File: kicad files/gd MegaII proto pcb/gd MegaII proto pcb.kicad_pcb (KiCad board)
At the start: 2 copper layers, 75 parts, among them J1 ABDIR, J2 ABEN, J3 FLIP, J4 DBDIR, J5 DBEN, J6 VGC Extra, J7 Bald-Ext-1, J8 VGC Extra, J9 Address, U1 Apple_MEGA_II, U2 DRAM64KX4, U3 74HCT245, U4 DRAM64KX4, U5 74HCT245, U6 74HCT86, U7 DRAM64KX4, U8 74HCT245, U9 DRAM64KX4

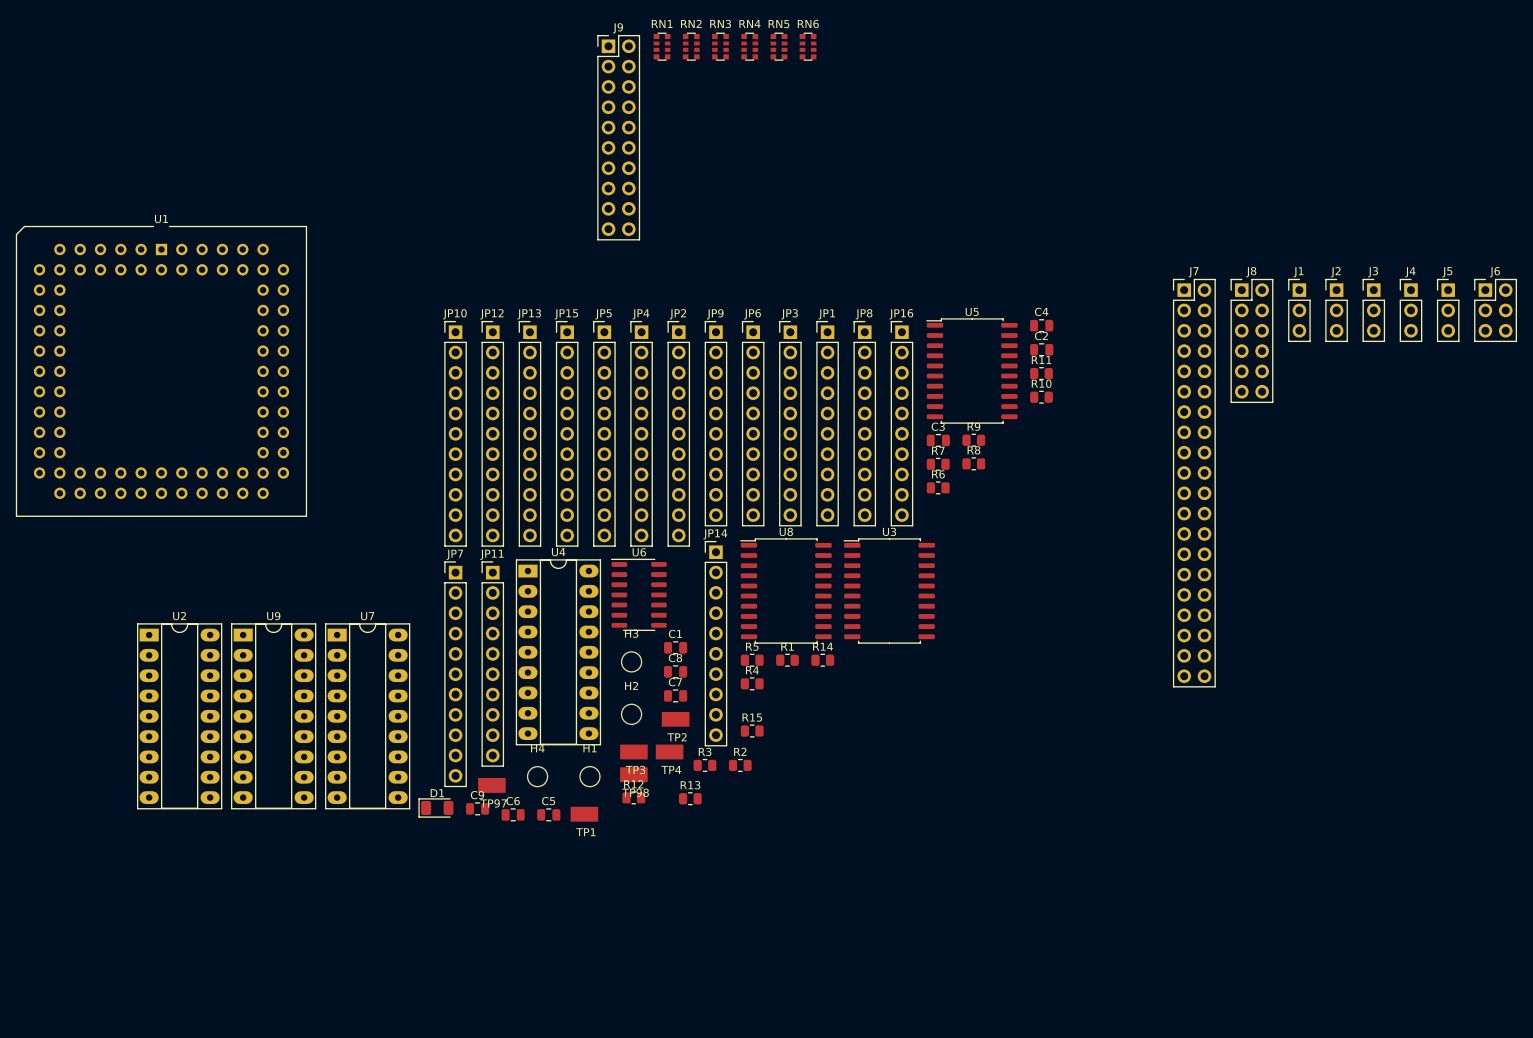
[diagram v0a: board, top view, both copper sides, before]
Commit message: MegaII 0 unrouted but 40+ DRC errors. KiCad doesn't like any of my via placements.
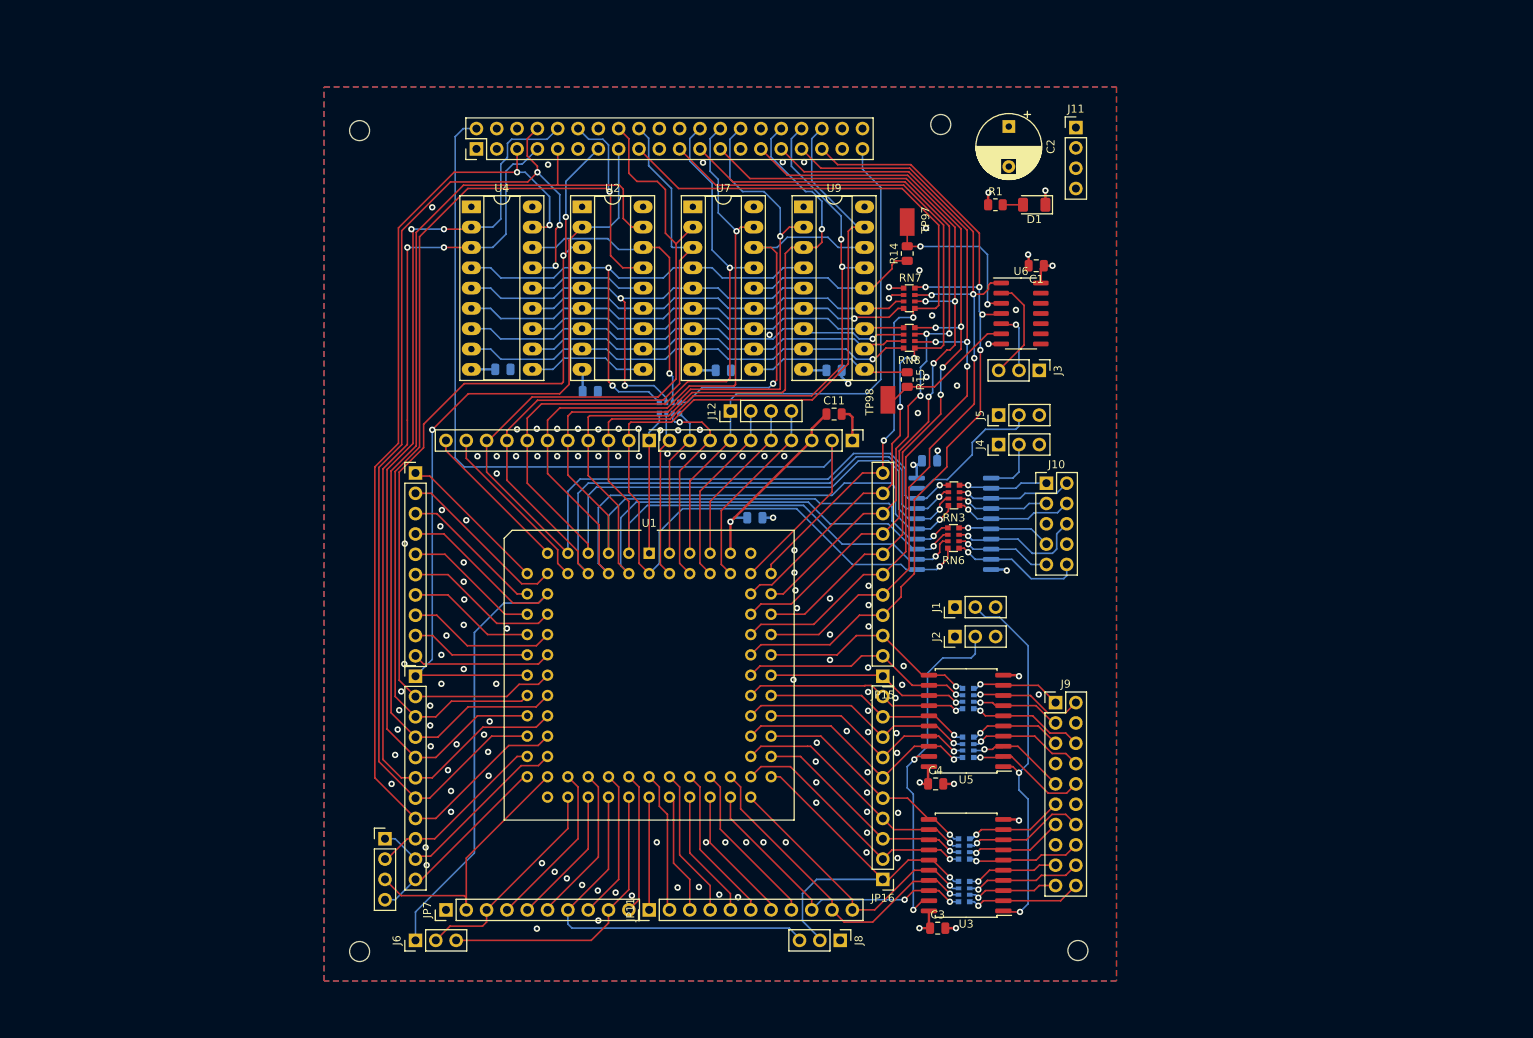
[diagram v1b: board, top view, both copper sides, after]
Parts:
- removed JP10, JP2: P22-32, Connector_PinHeader_2.54mm:PinHeader_1x11_P2.54mm_Vertical
- removed JP13, JP5: P43-53, Connector_PinHeader_2.54mm:PinHeader_1x11_P2.54mm_Vertical
- removed JP14, JP6: P75-84, Connector_PinHeader_2.54mm:PinHeader_1x10_P2.54mm_Vertical
- removed JP9: P12-21, Connector_PinHeader_2.54mm:PinHeader_1x10_P2.54mm_Vertical
- removed R10, R11, R12, R13, R2, R3, R4, R5, R6, R7, R8, R9: 100, Resistor_SMD:R_0805_2012Metric
- removed TP1, TP2, TP3, TP4: TestPoint, My Libraries:Harwin-S1751-46-Test-Point
- added C10: 10uF, Capacitor_SMD:C_0805_2012Metric, B.Cu at (142.7, 86.9)
- added C11: 1uF, Capacitor_SMD:C_0805_2012Metric, F.Cu at (152.7, 73.9)
- added J10: Data, Connector_PinHeader_2.54mm:PinHeader_2x05_P2.54mm_Vertical, F.Cu at (179.2, 82.5)
- added J11: PWR, Connector_PinHeader_2.54mm:PinHeader_1x04_P2.54mm_Vertical, F.Cu at (182.9, 38.1)
- added J12: CLKS, Connector_PinHeader_2.54mm:PinHeader_1x04_P2.54mm_Vertical, F.Cu at (139.7, 73.5)
- added RN7: 100, Resistor_SMD:R_Array_Convex_4x0612, F.Cu at (162.1, 59.4)
- added RN8: 100, Resistor_SMD:R_Array_Convex_4x0612, F.Cu at (162.1, 64.4)
- added RN9: 100, Resistor_SMD:R_Array_Convex_4x0612, B.Cu at (132.1, 73.2)
- C2: value 10uF -> 100uF; footprint Capacitor_SMD:C_0805_2012Metric -> Capacitor_THT:CP_Radial_D8.0mm_P5.00mm
- C5, C6, C7, C8, C9, RN1, RN2, RN4, RN5, U8: moved to B.Cu
- J6: value VGC Extra -> VGC Extra 1; footprint Connector_PinHeader_2.54mm:PinHeader_2x03_P2.54mm_Vertical -> Connector_PinHeader_2.54mm:PinHeader_1x03_P2.54mm_Vertical
- J8: value VGC Extra -> VGC Extra 2; footprint Connector_PinHeader_2.54mm:PinHeader_2x06_P2.54mm_Vertical -> Connector_PinHeader_2.54mm:PinHeader_1x03_P2.54mm_Vertical
- JP1: value P12-21 -> RGB Binary; footprint Connector_PinHeader_2.54mm:PinHeader_1x10_P2.54mm_Vertical -> Connector_PinHeader_2.54mm:PinHeader_1x04_P2.54mm_Vertical
- JP11: value P33-42 -> P64-74; footprint Connector_PinHeader_2.54mm:PinHeader_1x10_P2.54mm_Vertical -> Connector_PinHeader_2.54mm:PinHeader_1x11_P2.54mm_Vertical
- JP12: value P01-11 -> P54-63; footprint Connector_PinHeader_2.54mm:PinHeader_1x11_P2.54mm_Vertical -> Connector_PinHeader_2.54mm:PinHeader_1x10_P2.54mm_Vertical
- JP3: value P33-42 -> P54-63
- JP4: value P01-11 -> P64-74
- JP7: value P64-74 -> P54-63; footprint Connector_PinHeader_2.54mm:PinHeader_1x11_P2.54mm_Vertical -> Connector_PinHeader_2.54mm:PinHeader_1x10_P2.54mm_Vertical
- JP8: value P54-63 -> P64-74; footprint Connector_PinHeader_2.54mm:PinHeader_1x10_P2.54mm_Vertical -> Connector_PinHeader_2.54mm:PinHeader_1x11_P2.54mm_Vertical
- moved J6 156.5 mm to (100.3, 139.7), turned to 90 degrees
- moved RN5 108.1 mm to (168.9, 133.6), turned to 180 degrees
- moved D1 106.1 mm to (177.7, 47.8), turned to 180 degrees
- moved RN2 105.9 mm to (168.9, 128.3), turned to 180 degrees
- moved J9 99.3 mm to (180.3, 110.0)
- moved J8 95.5 mm to (153.4, 139.7), turned to 270 degrees
- moved RN4 91.7 mm to (169.4, 115.6), turned to 180 degrees
- moved J7 90.2 mm to (108.0, 40.8), turned to 90 degrees
- moved RN1 90.0 mm to (169.4, 109.5), turned to 180 degrees
- moved U9 88.2 mm to (148.8, 48.0)
- moved TP97 87.5 mm to (161.8, 49.9), turned to 90 degrees
- moved JP1 84.1 mm to (96.5, 127.0)
- moved H2 83.2 mm to (166.0, 37.7)
- moved U2 76.1 mm to (121.2, 48.0)
- moved H3 74.6 mm to (93.3, 38.5)
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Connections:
- C1 pad 1: VDD -> +5V
- C2 pad 1: VDD -> +5V
- C3 pad 1: VDD -> +5V
- C4 pad 1: VDD -> +5V
- C5 pad 1: VDD -> +5V
- C6 pad 1: VDD -> +5V
- C7 pad 1: VDD -> +5V
- C8 pad 1: VDD -> +5V
- C9 pad 1: VDD -> +5V
- J1 pad 1: VDD -> +5V
- J2 pad 1: VDD -> +5V
- J4 pad 1: VDD -> +5V
- J5 pad 1: VDD -> +5V
- J6 pad 2: /IRQ -> /RESET
- J6 pad 3: /RESET -> /R-W
- J7 pad 30: Net-(J7-Pad30) -> GND
- J8 pad 1: Net-(J8-Pad1) -> GND
- J8 pad 2: Net-(J8-Pad2) -> /BA12
- J8 pad 3: Net-(J8-Pad3) -> /M2SEL
- JP1 pad 1: /SPKR -> /RGB4
- JP1 pad 2: /KSEL1 -> /RGB8
- JP1 pad 3: /KSEL2 -> /RGB1
- JP1 pad 4: /IRQ -> /RGB2
- JP11 pad 1: GND -> /S1
- JP11 pad 10: /S0 -> /BA14
- JP11 pad 2: /RGB1 -> /S2
- JP11 pad 3: /RESET -> /S3
- JP11 pad 4: /MDI-MDO -> /S4
- JP11 pad 5: /RCMEN -> /S5
- JP11 pad 6: /DMA -> /RMBK
- JP11 pad 7: /M2SEL -> /WINDOW
- JP11 pad 8: /INH -> /SYNC
- JP11 pad 9: /R-W -> /BA15
- JP12 pad 1: /RAMWE -> GND
- JP12 pad 10: /PDLTRIG -> /RAS
- JP12 pad 2: /MD7 -> /14M
- JP12 pad 3: /MD6 -> +5V
- JP12 pad 4: /MD5 -> /7M
- JP12 pad 5: /MD4 -> /CREF
- JP12 pad 6: /MD3 -> /Q3
- JP12 pad 7: /MD2 -> /PH#
- JP12 pad 8: /MD1 -> /CASA
- JP12 pad 9: /MD0 -> /CASM
- JP15 pad 1: /A2 -> /BA2
- JP15 pad 2: /A1 -> /BA1
- JP15 pad 3: /A0 -> /BA0
- JP16 pad 1: /A12 -> /BA12
- JP16 pad 10: /A3 -> /BA3
- JP16 pad 2: /A11 -> /BA11
- JP16 pad 3: /A10 -> /BA10
- JP16 pad 4: /A9 -> /BA9
- JP16 pad 5: /A8 -> /BA8
- JP16 pad 6: /A7 -> /BA7
- JP16 pad 7: /A6 -> /BA6
- JP16 pad 8: /A5 -> /BA5
- JP16 pad 9: /A4 -> /BA4
- JP3 pad 1: GND -> /SPKR
- JP3 pad 10: /S0 -> /SERVIDEO
- JP3 pad 2: /RGB1 -> /KSEL1
- JP3 pad 3: /RESET -> /KSEL2
- JP3 pad 4: /MDI-MDO -> /IRQ
- JP3 pad 5: /RCMEN -> /X0
- JP3 pad 6: /DMA -> /X1
- JP3 pad 7: /M2SEL -> /Y0
- JP3 pad 8: /INH -> /Y1
- JP3 pad 9: /R-W -> /MSW
- JP4 pad 1: /RAMWE -> /AD0
- JP4 pad 10: /PDLTRIG -> /RGB4
- JP4 pad 11: /C060-67 -> /RGB2
- JP4 pad 2: /MD7 -> /AD1
- JP4 pad 3: /MD6 -> /AD2
- JP4 pad 4: /MD5 -> /AD3
- JP4 pad 5: /MD4 -> /AD4
- JP4 pad 6: /MD3 -> /AD5
- JP4 pad 7: /MD2 -> /AD6
- JP4 pad 8: /MD1 -> /AD7
- JP4 pad 9: /MD0 -> /RGB8
- JP7 pad 1: /A2 -> GND
- JP7 pad 10: /RA1 -> /S0
- JP7 pad 2: /A1 -> /RGB1
- JP7 pad 3: /A0 -> /RESET
- JP7 pad 4: /RA7 -> /MDI-MDO
- JP7 pad 5: /RA6 -> /ROMEN
- JP7 pad 6: /RA5 -> /DMA
- JP7 pad 7: /RA4 -> /M2SEL
- JP7 pad 8: /RA3 -> /INH
- JP7 pad 9: /RA2 -> /R-W
- JP8 pad 1: /A12 -> /RAMWE
- JP8 pad 10: /A3 -> /PDLTRIG
- JP8 pad 2: /A11 -> /MD7
- JP8 pad 3: /A10 -> /MD6
- JP8 pad 4: /A9 -> /MD5
- JP8 pad 5: /A8 -> /MD4
- JP8 pad 6: /A7 -> /MD3
- JP8 pad 7: /A6 -> /MD2
- JP8 pad 8: /A5 -> /MD1
- JP8 pad 9: /A4 -> /MD0
- R1 pad 1: VDD -> +5V
- RN3 pad 1: /D0 -> /D3
- RN3 pad 2: /D1 -> /D2
- RN3 pad 3: /D2 -> /D1
- RN3 pad 4: /D3 -> /D0
- RN3 pad 5: /MD3 -> /MD0
- RN3 pad 6: /MD2 -> /MD1
- RN3 pad 7: /MD1 -> /MD2
- RN3 pad 8: /MD0 -> /MD3
- RN6 pad 1: /D4 -> /D7
- RN6 pad 2: /D5 -> /D6
- RN6 pad 3: /D6 -> /D5
- RN6 pad 4: /D7 -> /D4
- RN6 pad 5: /MD7 -> /MD4
- RN6 pad 6: /MD6 -> /MD5
- RN6 pad 7: /MD5 -> /MD6
- RN6 pad 8: /MD4 -> /MD7
- U1 pad 77: VDD -> +5V
- U2 pad 9: VDD -> +5V
- U3 pad 20: VDD -> +5V
- U4 pad 9: VDD -> +5V
- U5 pad 20: VDD -> +5V
- U6 pad 14: (no net) -> +5V
- U6 pad 7: (no net) -> GND
- U7 pad 9: VDD -> +5V
- U8 pad 11: /MD0 -> /MD7
- U8 pad 12: /MD1 -> /MD6
- U8 pad 13: /MD2 -> /MD5
- U8 pad 14: /MD3 -> /MD4
- U8 pad 15: /MD4 -> /MD3
- U8 pad 16: /MD5 -> /MD2
- U8 pad 17: /MD6 -> /MD1
- U8 pad 18: /MD7 -> /MD0
- U8 pad 2: /D7 -> /D0
- U8 pad 20: VDD -> +5V
- U8 pad 3: /D6 -> /D1
- U8 pad 4: /D5 -> /D2
- U8 pad 5: /D4 -> /D3
- U8 pad 6: /D3 -> /D4
- U8 pad 7: /D2 -> /D5
- U8 pad 8: /D1 -> /D6
- U8 pad 9: /D0 -> /D7
- U9 pad 9: VDD -> +5V
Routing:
- net /MD1: track 0.00 -> 147.7 mm, vias 0 -> 1
- net /MD0: track 0.00 -> 147.2 mm, vias 0 -> 1
- net /MD2: track 0.00 -> 145.5 mm, vias 0 -> 2
- net /MD3: track 0.00 -> 144.1 mm, vias 0 -> 2
- net /MD5: track 0.00 -> 140.1 mm, vias 0 -> 2
- net /MD4: track 0.00 -> 139.5 mm, vias 0 -> 2
- net /MD6: track 0.00 -> 134.2 mm, vias 0 -> 3
- net /AD6: track 0.00 -> 133.8 mm, vias 0 -> 3
- net /MD7: track 0.00 -> 133.2 mm, vias 0 -> 1
- net /AD7: track 0.00 -> 129.7 mm, vias 0 -> 2
- net /AD2: track 0.00 -> 127.1 mm, vias 0 -> 1
- net /AD3: track 0.00 -> 124.0 mm
- net /AD5: track 0.00 -> 116.0 mm, vias 0 -> 2
- net /14M: track 0.00 -> 114.4 mm
- net /AD4: track 0.00 -> 113.6 mm, vias 0 -> 2
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- added copper zone on In1.Cu, net +5V
- added copper zone on B.Cu, net GND
- added copper zone on F.Cu, net GND
- added copper zone on In2.Cu, net GND
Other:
- copper layers 2 -> 4
- net class Default: clearance 0.2 -> 0.1524; trace_width 0.25 -> 0.2032
- net class Power added: clearance 0.3048, trace_width 0.3048, via_dia 0.8, via_drill 0.4
- rule trace_clearance: 0.2 -> 0.1524
- rule trace_min: 0.2 -> 0.1524

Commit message: all three boards final, prepping for gerbers
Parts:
- added REF**: OSHW-Symbol_6.7x6mm_SilkScreen, Symbol:OSHW-Symbol_6.7x6mm_SilkScreen, F.Cu at (97.8, 62.0)
- added REF**: KiCad-Logo_8mm_SilkScreen, Symbol:KiCad-Logo_8mm_SilkScreen, B.Cu at (129.8, 107.4)
- added svg2mod: G***, My Libraries:BE10v2, F.Cu at (90.4, 38.6)
- moved H2 19.9 mm to (185.7, 35.1)
- moved J11 10.2 mm to (172.7, 36.8)
- moved C2 8.32 mm to (166.4, 39.8), turned to 180 degrees
- moved H1 4.58 mm to (185.7, 144.8)
- moved H4 3.79 mm to (92.5, 144.8)
- moved D1 3.69 mm to (179.3, 51.1)
- moved R1 3.69 mm to (174.5, 51.1)
- moved H3 3.50 mm to (92.6, 35.1)
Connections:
- J3 pad 1: GND -> /FLIP7
- J3 pad 2: /FLIP7 -> GND
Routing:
- net /FLIP7: track 7.77 -> 8.82 mm
- net GND: vias 136 -> 99
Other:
- board outline added: 98.8 x 115.3 mm
- board text added: "1"
- board text added: "10"
- board text added: "11"
- board text added: "12"
- board text added: "13"
- board text added: "14M"
- board text added: "2"
- board text added: "24"
- board text added: "32"
- board text added: "39"
- board text added: "43"
- board text added: "44"
- board text added: "5"
- board text added: "53"
- board text added: "54"
- board text added: "5V"
- board text added: "64"
- board text added: "7"
- board text added: "7M"
- board text added: "A0"
- board text added: "A1"
- board text added: "A10"
- board text added: "A11"
- board text added: "A12"
- board text added: "A13"
- board text added: "A14"
- board text added: "A15"
- board text added: "A2"
- board text added: "A3"
- board text added: "A4"
- board text added: "A5"
- board text added: "A6"
- board text added: "A7"
- board text added: "A8"
- board text added: "A9"
- board text added: "AB"
- board text added: "AD0"
- board text added: "AD1"
- board text added: "AD2"
- board text added: "AD3"
- board text added: "AD4"
- board text added: "AD5"
- board text added: "AD6"
- board text added: "AD7"
- board text added: "Address"
- board text added: "BA0"
- board text added: "BA1"
- board text added: "BA10"
- board text added: "BA11"
- board text added: "BA12"
- board text added: "BA13"
- board text added: "BA14"
- board text added: "BA15"
- board text added: "BA2"
- board text added: "BA3"
- board text added: "BA4"
- board text added: "BA5"
- board text added: "BA6"
- board text added: "BA7"
- board text added: "BA8"
- board text added: "BA9"
- board text added: "C060"
- board text added: "CASA"
- board text added: "CASM"
- board text added: "CREF"
- board text added: "D0"
- board text added: "D1"
- board text added: "D2"
- board text added: "D3"
- board text added: "D4"
- board text added: "D5"
- board text added: "D6"
- board text added: "D7"
- board text added: "DB"
- board text added: "DIR"
- board text added: "DMA"
- board text added: "Data"
- board text added: "EN"
- board text added: "Flip6"
- board text added: "Flip7"
- board text added: "INH"
- board text added: "IRQ"
- board text added: "KSEL1"
- board text added: "KSEL2"
- board text added: "M2SEL"
- board text added: "MD0"
- board text added: "MD1"
- board text added: "MD2"
- board text added: "MD3"
- board text added: "MD4"
- board text added: "MD5"
- board text added: "MD6"
- board text added: "MD7"
- board text added: "MDI-MDO"
- board text added: "MSW"
- board text added: "NC"
- board text added: "PDL"
- board text added: "PH#"
- board text added: "Q3"
- board text added: "RA0"
- board text added: "RA1"
- board text added: "RA2"
- board text added: "RA3"
- board text added: "RA4"
- board text added: "RA5"
- board text added: "RA6"
- board text added: "RA7"
- board text added: "RAMWE"
- board text added: "RAS"
- board text added: "RGB1"
- board text added: "RGB2"
- board text added: "RGB4"
- board text added: "RGB8"
- board text added: "RMBK"
- board text added: "ROMEN"
- board text added: "RW"
- board text added: "S0"
- board text added: "S1"
- board text added: "S2"
- board text added: "S3"
- board text added: "S4"
- board text added: "S5"
- board text added: "SERVID"
- board text added: "SPKR"
- board text added: "SYNC"
- board text added: "This board (and this project) would not happen without the help of rjhelms. Thank you!"
- board text added: "U2"
- board text added: "U4"
- board text added: "U7"
- board text added: "U9"
- board text added: "WNDW"
- board text added: "X0"
- board text added: "X1"
- board text added: "Y0"
- board text added: "Y1"
- board text added: "gd MEGA-][ @baldengineer rev1"
- board text added: "~RES"
